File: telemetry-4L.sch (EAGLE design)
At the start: 68 parts, among them SW1 MF-SW-TACT-4.2MM, U1 ATSAMD21G18A-MUT, U2 SPX3819M5-L-3-0, U3 MCP73831T-2ACI/OT, U5 SIM868, U6 BMP280, U7 BNO055, X1 S2B-PH-SM4-TB(LF)(SN), X2 FC-135 32.7680KA-A3, X3 MF-CON-MICROUSB-RIGHT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

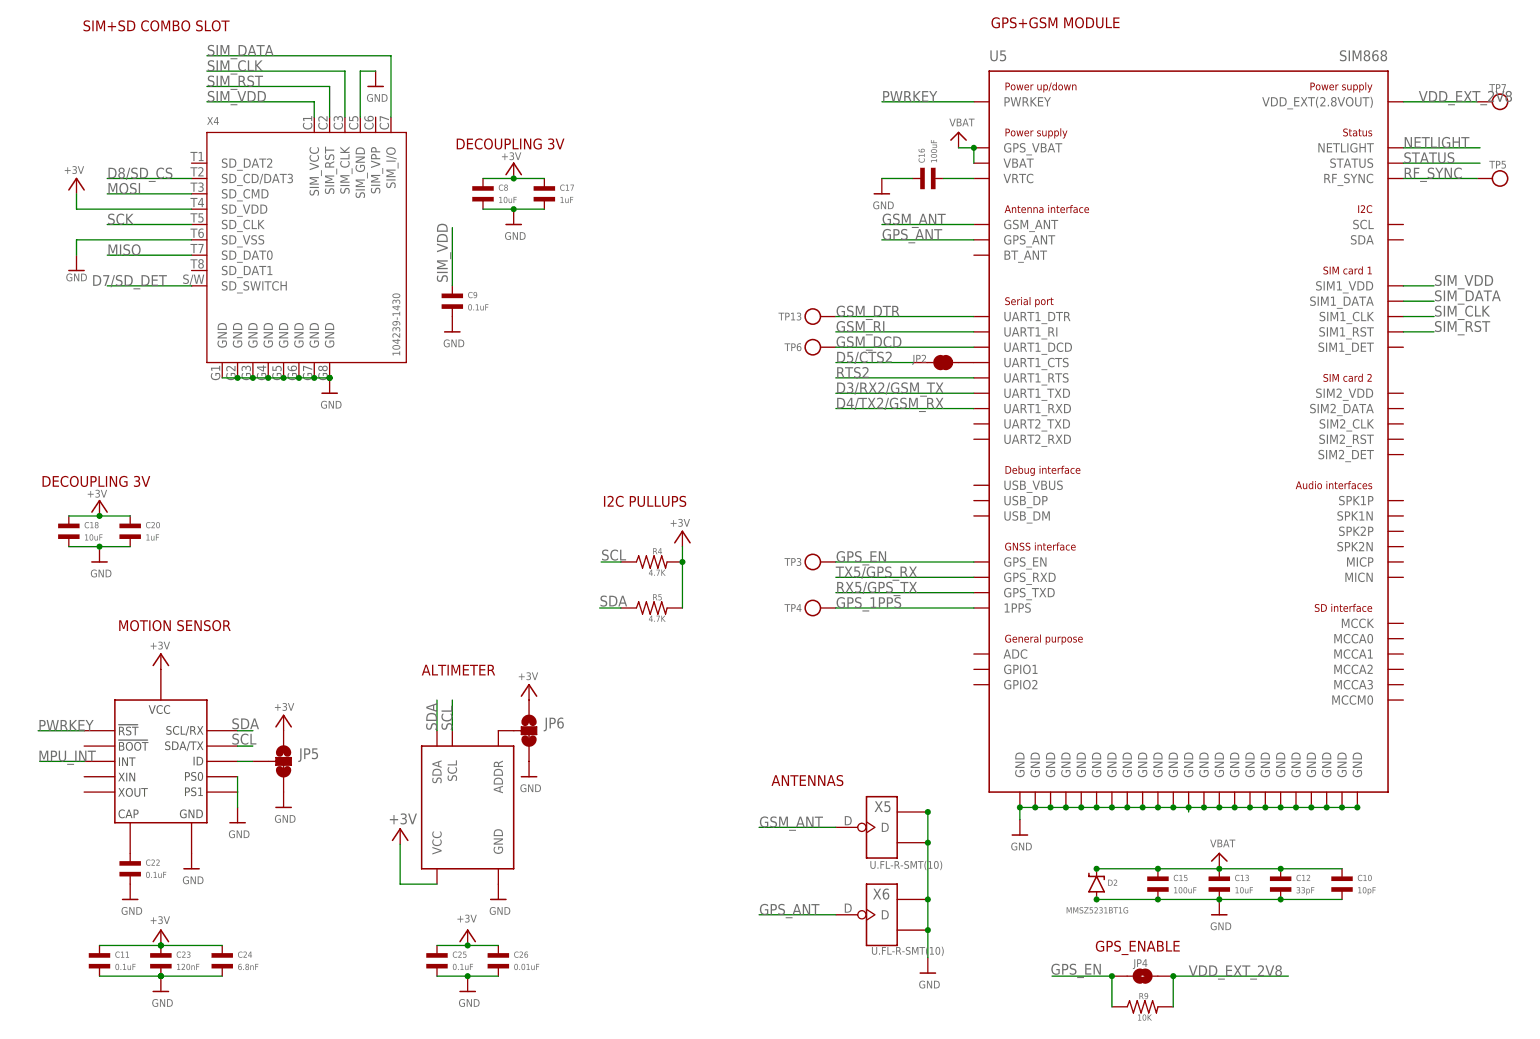
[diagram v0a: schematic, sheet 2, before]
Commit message: Working on 4-layer version
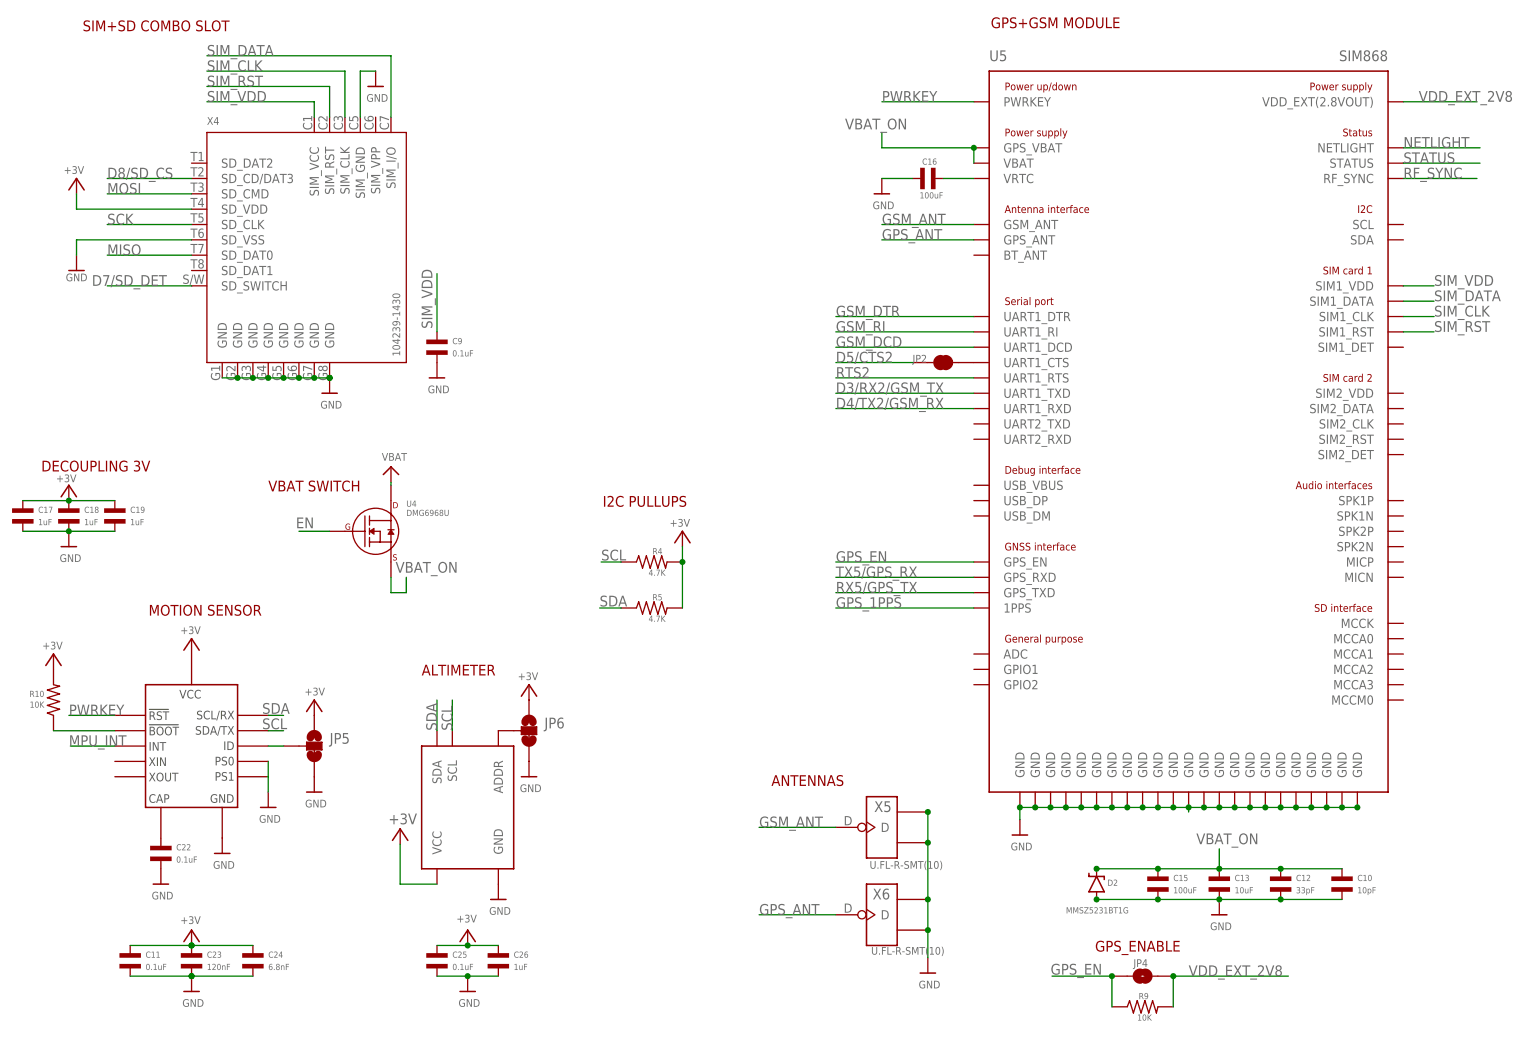
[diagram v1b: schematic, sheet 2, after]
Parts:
- removed C20: 1uF, MF_Passives:CAPACITOR_NP_0402
- removed C8: 10uF, MF_Passives:CAPACITOR_NP_0603
- removed TP13, TP3, TP4, TP5, TP6, TP7: (no value), microbuilder:TESTPOINTROUND1.5MM
- added C19: 1uF, MF_Passives:CAPACITOR_NP_0402
- added JP7: JUMPER-PAD-2-NOYES_SILK, SparkFun-Passives:JUMPER-PAD-2-NOYES_SILK
- added JP8: JUMPER-PAD-2-NC_BY_TRACE, SparkFun-Passives:JUMPER-PAD-2-NC_BY_TRACE
- added R10: 10K, MF_Passives:RESISTOR_0402
- added SW2: SWITCH_SPDT, SparkFun-Electromechanical:SWITCH_SPDT
- added U4: DMG6968U, MF_Discrete_Semiconductor:N-CHANNEL_FET_SOT-23-3
- C18: value 10uF -> 1uF; device MF_Passives:CAPACITOR_NP_0603 -> MF_Passives:CAPACITOR_NP_0402
- C26: value 0.01uF -> 1uF
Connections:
- new net N$11: R1.P$2, SW2.P
- new net N$12: JP7.2, SW2.O
- new net N$13: JP8.2, SW2.S
- new net N$14: R10.P$1, U7.BOOT
- new net VBAT_ON: C10.P$1, C12.P$1, C13.P$1, C15.P$1, D2.C, U4.SOURCE, U5.GPS_VBAT, U5.VBAT
- net +3V: now also C19.P$1, R10.P$2; no longer C20.P$1, C8.P$1
- net EN: now also R1.P$1, U4.GATE; no longer R1.P$2
- net GND: now also C19.P$2, JP7.1; no longer C20.P$2, C8.P$2
- net GPS_1PPS: no longer TP4.P$1
- net GPS_EN: no longer TP3.P$1
- net GSM_DCD: no longer TP6.P$1
- net GSM_DTR: no longer TP13.P$1
- net RF_SYNC: no longer TP5.P$1
- net VBAT: now also JP8.1, U4.DRAIN; no longer C10.P$1, C12.P$1, C13.P$1, C15.P$1, D2.C, U5.GPS_VBAT, U5.VBAT
- net VBUS: no longer R1.P$1
- net VDD_EXT_2V8: no longer TP7.P$1
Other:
- note added: "ON/OFF SWITCH"
- note added: "VBAT SWITCH"
- moved on the sheet: C11, C17, C18, C22, C23, C24, C9, D1, JP5, R1

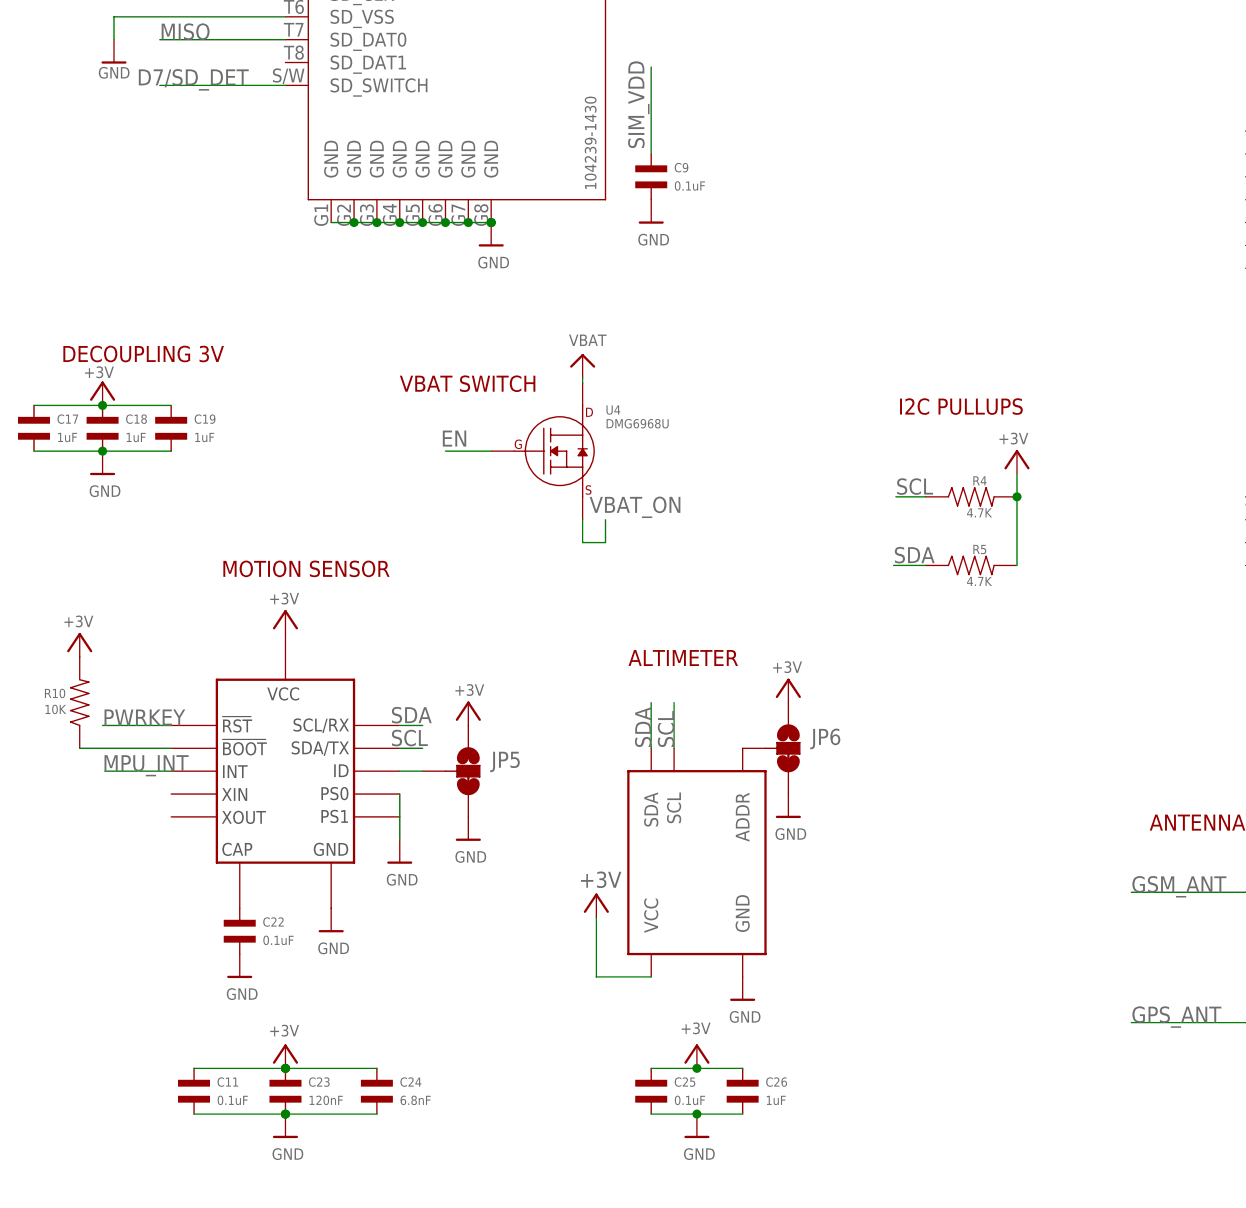
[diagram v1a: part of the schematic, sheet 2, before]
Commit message: Switched to MPU-9250 IMU
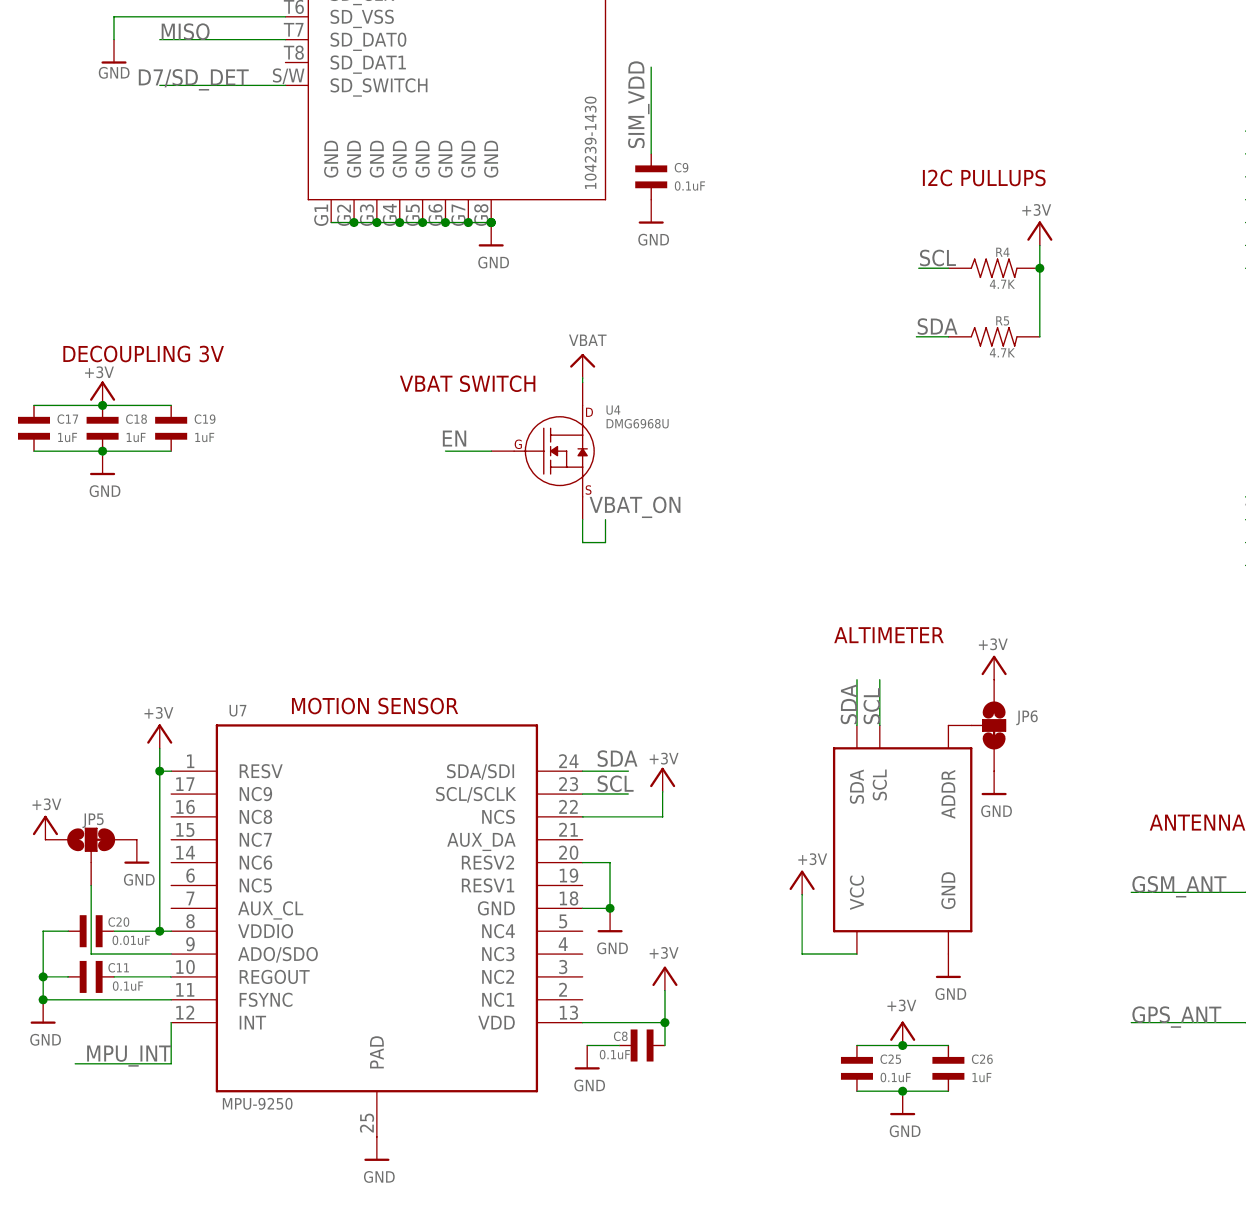
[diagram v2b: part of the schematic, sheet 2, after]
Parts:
- removed C22: 0.1uF, MF_Passives:CAPACITOR_NP_0402
- removed C23: 120nF, MF_Passives:CAPACITOR_NP_0402
- removed C24: 6.8nF, MF_Passives:CAPACITOR_NP_0402
- removed R10: 10K, MF_Passives:RESISTOR_0402
- added C20: 0.01uF, MF_Passives:CAPACITOR_NP_0402
- added C8: 0.1uF, MF_Passives:CAPACITOR_NP_0402
- U7: value BNO055 -> MPU-9250; device alvaroferran:BNO055 -> misc:MPU-9250
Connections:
- removed net N$14: R10.P$1, U7.BOOT
- removed net N$9: JP5.2, U7.ID
- new net N$23: C11.P$2, U7.REGOUT
- net +3V: now also C20.P$2, C8.P$2, U7.NCS, U7.RESV, U7.VDD, U7.VDDIO; no longer C11.P$1, C23.P$1, C24.P$1, R10.P$2, U7.VCC
- net GND: now also C11.P$1, C20.P$1, C8.P$1, U7.FSYNC, U7.PAD, U7.RESV2; no longer C11.P$2, C22.P$2, C23.P$2, C24.P$2, U7.PS0, U7.PS1
- net N$2: now also JP5.2, U7.ADO/SDO; no longer C22.P$1, U7.CAP
- net PWRKEY: no longer U7.RST
- net SCL: now also U7.SCL/SCLK; no longer U7.SDA/TX
- net SDA: now also U7.SDA/SDI; no longer U7.SCL/RX
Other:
- moved on the sheet: C11, C25, C26, JP5, JP6, R4, R5

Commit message: Some work on routing
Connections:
- net VBAT: no longer R3.P$1
- net VBAT_ON: now also R3.P$1
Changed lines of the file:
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@@
 <part name="U$48" library="microbuilder" deviceset="GND" device=""/>
 <part name="JP2" library="SparkFun-Passives" deviceset="JUMPER-PAD-2-NC_BY_TRACE" device=""/>
-<part name="U$2" library="microbuilder" deviceset="VBAT" device=""/>
 <part name="U6" library="BMP280" deviceset="BMP280" device=""/>
 <part name="U$54" library="microbuilder" deviceset="GND" device=""/>
@@
 <instance part="TP1" gate="G$1" x="121.92" y="17.78" rot="R270"/>
 <instance part="TP2" gate="G$1" x="121.92" y="15.24" rot="R270"/>
-<instance part="U$2" gate="G$1" x="246.38" y="121.92"/>
 <instance part="D3" gate="G$1" x="242.824" y="52.07" rot="R270"/>
 <instance part="D4" gate="G$1" x="162.306" y="142.24" smashed="yes">
@@
 </segment>
 <segment>
-<pinref part="R3" gate="G$1" pin="P$1"/>
-<pinref part="U$2" gate="G$1" pin="VBAT"/>
-</segment>
-<segment>
 <pinref part="U$44" gate="G$1" pin="VBAT"/>
 <pinref part="JP8" gate="G$1" pin="1"/>
@@
 </segment>
 </net>
+<net name="VBAT_ON" class="0">
+<segment>
+<pinref part="R3" gate="G$1" pin="P$1"/>
+<wire x1="246.38" y1="119.38" x2="246.38" y2="121.666" width="0.1524" layer="91"/>
+<label x="246.38" y="121.92" size="1.778" layer="95"/>
+</segment>
+</net>

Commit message: Worked on it
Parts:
- added J1: (no value), microbuilder:TERMBLOCK_1X2
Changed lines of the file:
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@@
 <part name="U$25" library="microbuilder" deviceset="GND" device=""/>
 <part name="U$26" library="microbuilder" deviceset="GND" device=""/>
+<part name="J1" library="microbuilder" deviceset="TERMBLOCK_1X2" device=""/>
 </parts>
 <sheets>
@@
 <instance part="U$25" gate="G$1" x="8.636" y="22.86"/>
 <instance part="U$26" gate="G$1" x="19.05" y="40.64"/>
+<instance part="J1" gate="G$1" x="106.68" y="149.86"/>
 </instances>
 <busses>
